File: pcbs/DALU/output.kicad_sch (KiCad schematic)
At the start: 5 parts, among them U601 74HCT541, U602 74HCT541, U603 74LS540, U604 74HCT541, U605 74HCT541

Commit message: Rethinking some design
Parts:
- removed U601, U602, U604, U605: 74HCT541, Package_DIP:DIP-20_W7.62mm_Socket, symbol 74xx:74HCT541
- removed U603: 74LS540, Package_DIP:DIP-20_W7.62mm_Socket, symbol 74xx:74LS540
- added R601: 10k, Resistor_THT:R_Axial_DIN0207_L6.3mm_D2.5mm_P7.62mm_Horizontal, symbol Device:R
- added RN601: R_Network08, Resistor_THT:R_Array_SIP9, symbol Device:R_Network08
- added U601: 74HC74, symbol 74xx:74HC74
- added U602: 74LS573, Package_DIP:DIP-20_W7.62mm_Socket, symbol 74xx:74LS573
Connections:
- net +5V: now also U601.1 (~{R}), U601.10 (~{S}), U601.13 (~{R}), U601.14 (VCC), U601.4 (~{S}), U602.20 (VCC)
- net GND: now also R601.2, RN601.1 (common), U601.11 (C), U601.12 (D), U601.7 (GND), U602.10 (GND)
- new net: U601.3 (C), U602.11 (Load)
- new net: RN601.9 (R8), U602.2 (D0)
- new net: RN601.8 (R7), U602.3 (D1)
- new net: RN601.7 (R6), U602.4 (D2)
- new net: RN601.6 (R5), U602.5 (D3)
- new net: RN601.5 (R4), U602.6 (D4)
- new net: RN601.4 (R3), U602.7 (D5)
- new net: RN601.3 (R2), U602.8 (D6)
- new net: RN601.2 (R1), U602.9 (D7)
- new net DALUFLAG: U601.5 (Q)
- new net FLAG: R601.1, U601.2 (D)
- no-connect marks 0 -> 3

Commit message: Thinking about some of the control logic
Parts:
- added D601, D602: 1N4148, Diode_THT:D_DO-35_SOD27_P7.62mm_Horizontal, symbol Diode:1N4148
- added R601, R603, R604: 100k, Resistor_THT:R_Axial_DIN0207_L6.3mm_D2.5mm_P7.62mm_Horizontal, symbol Device:R
- added R602: 10k, Resistor_THT:R_Axial_DIN0207_L6.3mm_D2.5mm_P7.62mm_Horizontal, symbol Device:R
- added U602: 74HC125, Package_DIP:DIP-14_W7.62mm_Socket, symbol 74xx:74LS125
- U601: footprint (none) -> Package_DIP:DIP-14_W7.62mm_Socket
- renumbered R601 to R605, U602 to U603
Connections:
- net +5V: now also R604.1, U602.14 (VCC), U602.5
- net GND: now also R601.2, R602.2, R603.1, U602.7 (GND)
- net CLK: now reaches U601.3 (C), U603.11 (Load)
- net CLK: now also R602.1, U602.3
- net at U603.1 (OE): now also R604.2, U602.8
- new net: D601.1 (K), D602.1 (K), R601.1, U602.4
- new net: R603.2, U602.10, U602.6
- new net Commit: D602.2 (A)
- new net Execute: D601.2 (A), U602.2
- new net ~{ACTIVE_{DALU}}: U602.1, U602.9
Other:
- note added: "Only one of Decode, Execute and Commit will be high at any given time"
- moved on the sheet: U601B

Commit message: Thinking about SMD assembly. Will be rethinking
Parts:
- removed U603: 74LS573, Package_DIP:DIP-20_W7.62mm_Socket, symbol 74xx:74LS573
- added U603: 74HCT574, Package_SO:SOIC-20W_7.5x12.8mm_P1.27mm, symbol 74xx:74HCT574
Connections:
- net +5V: now also U603.20 (VCC)
- net CLK: now also U603.11 (Cp)
- net GND: now also U603.10 (GND)
- net at R604.2, U602.8: now also U603.1 (OE)
- net at RN601.9 (R8): now also U603.2 (D0)
- net at RN601.8 (R7): now also U603.3 (D1)
- net at RN601.7 (R6): now also U603.4 (D2)
- net at RN601.6 (R5): now also U603.5 (D3)
- net at RN601.5 (R4): now also U603.6 (D4)
- net at RN601.4 (R3): now also U603.7 (D5)
- net at RN601.3 (R2): now also U603.8 (D6)
- net at RN601.2 (R1): now also U603.9 (D7)

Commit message: Doing some rethinking
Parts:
- U703: renamed from U603; footprint Package_SO:SOIC-20W_7.5x12.8mm_P1.27mm -> Package_DIP:DIP-20_W7.62mm_Socket; LCSC C435813 -> (none)
- renumbered D601 to D701, D602 to D702, R601 to R701, R602 to R702, R603 to R703, R604 to R704, R605 to R705, RN601 to RN701, U601 to U701, U602 to U702

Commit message: Starting to think about decoding etc.
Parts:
- removed D701, D702: 1N4148, Diode_THT:D_DO-35_SOD27_P7.62mm_Horizontal, symbol Diode:1N4148
- removed R701, R703, R704: 100k, Resistor_THT:R_Axial_DIN0207_L6.3mm_D2.5mm_P7.62mm_Horizontal, symbol Device:R
- removed R702: 10k, Resistor_THT:R_Axial_DIN0207_L6.3mm_D2.5mm_P7.62mm_Horizontal, symbol Device:R
- removed U702: 74HC125, Package_DIP:DIP-14_W7.62mm_Socket, symbol 74xx:74LS125
- renumbered R705 to R801, RN701 to RN801, U701 to U801, U703 to U802
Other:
- note removed: "Only one of Decode, Execute and Commit will be high at any given time"

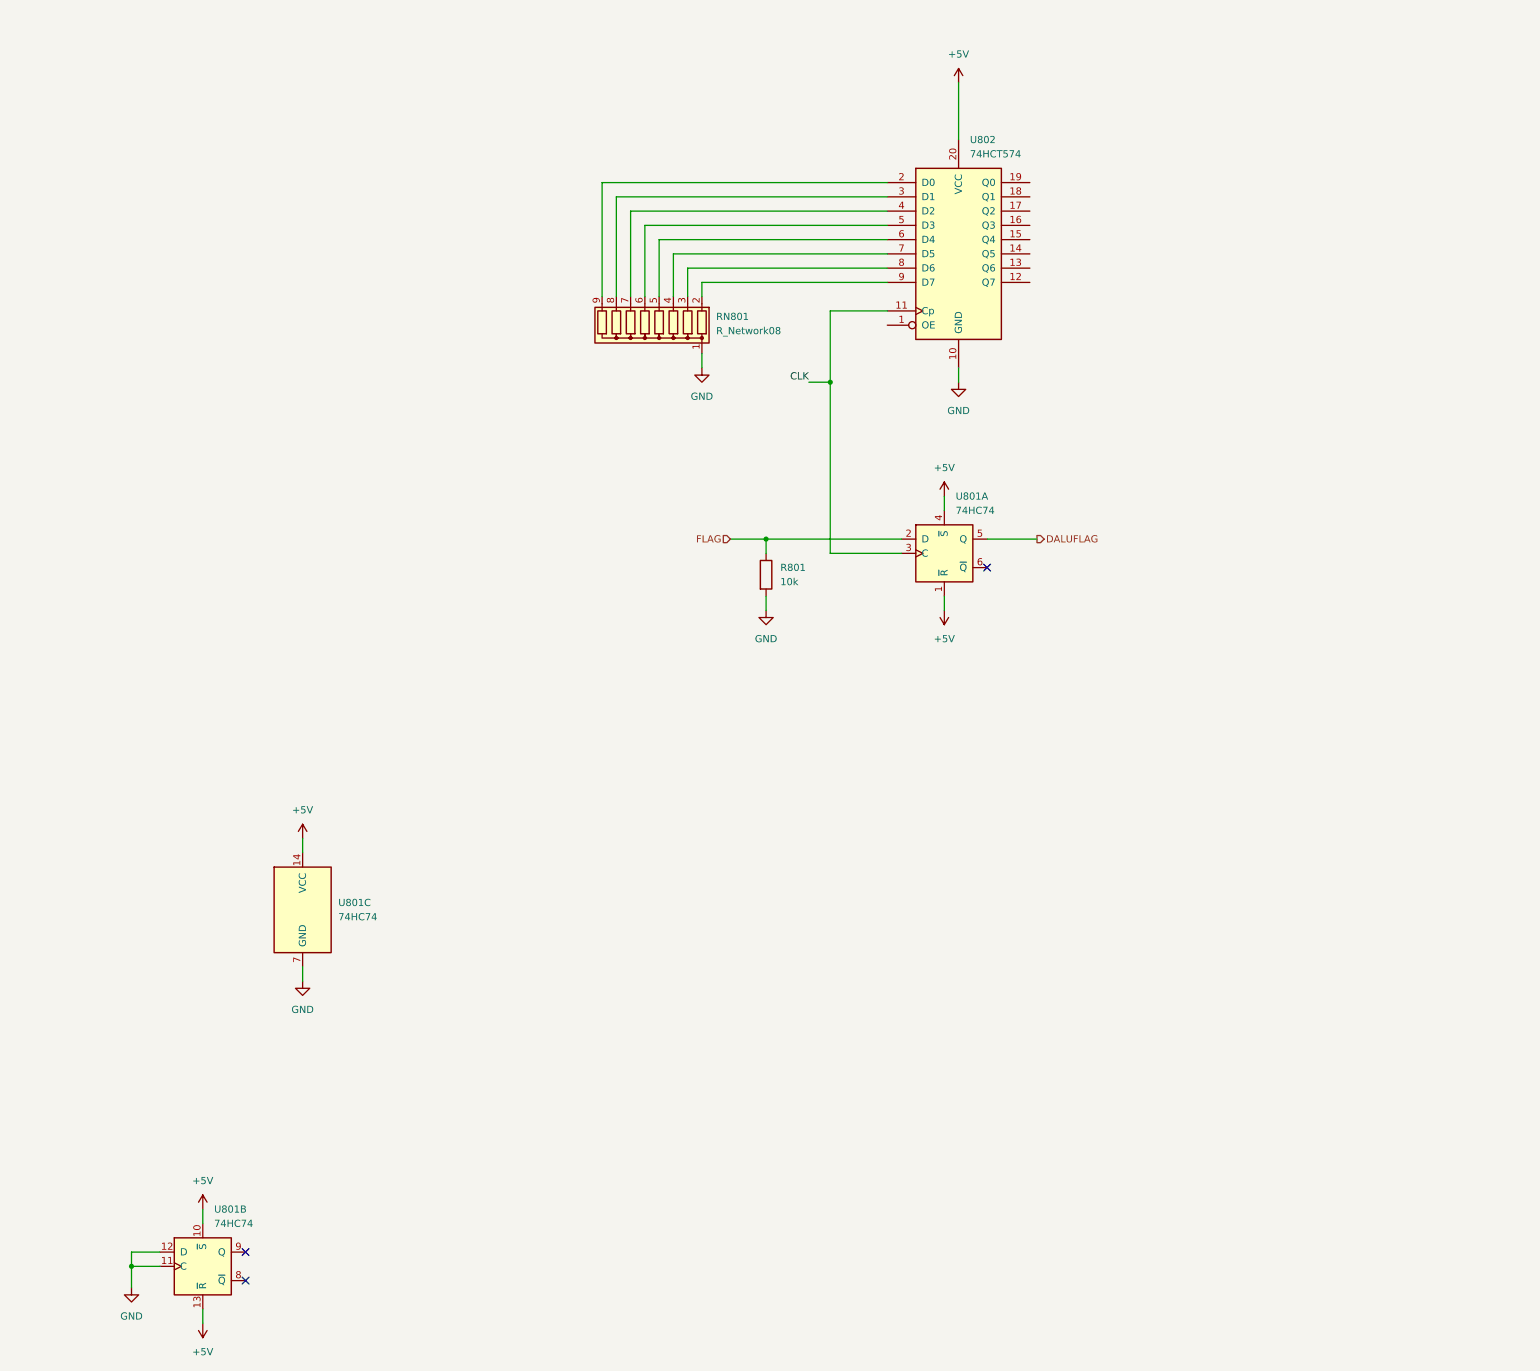
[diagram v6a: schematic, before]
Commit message: Starting to do the routing. Schematic not yet complete, though
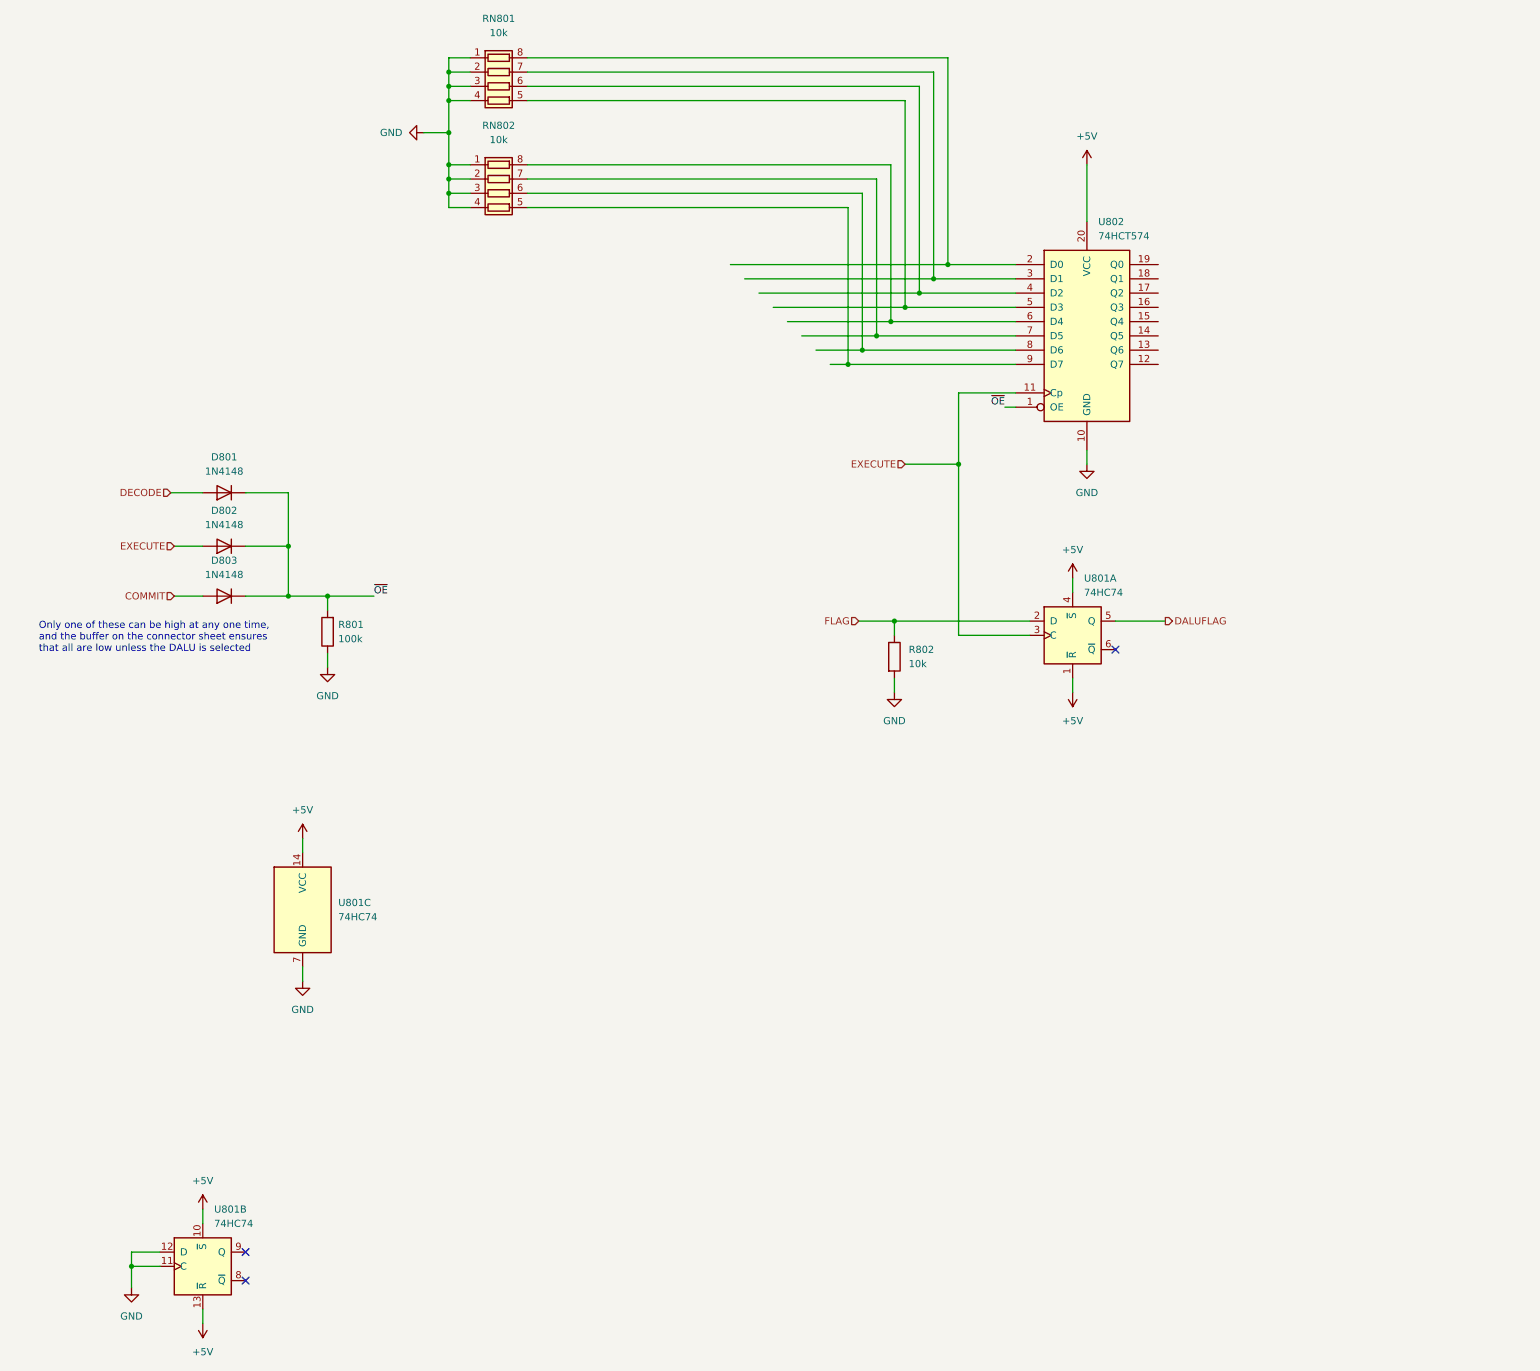
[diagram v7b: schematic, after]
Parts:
- removed RN801: R_Network08, Resistor_THT:R_Array_SIP9, symbol Device:R_Network08
- added D801, D802, D803: 1N4148, Diode_THT:D_DO-35_SOD27_P7.62mm_Horizontal, symbol Diode:1N4148
- added R801: 100k, Resistor_THT:R_Axial_DIN0207_L6.3mm_D2.5mm_P7.62mm_Horizontal, symbol Device:R
- added RN801, RN802: 10k, Resistor_SMD:R_Array_Convex_4x0402, symbol Device:R_Pack04
- renumbered R801 to R802
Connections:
- net GND: now also R801.1, RN801.1 (R1.1), RN801.2 (R2.1), RN801.3 (R3.1), RN801.4 (R4.1), RN802.1 (R1.1), RN802.2 (R2.1), RN802.3 (R3.1), RN802.4 (R4.1)
- net at U802.9 (D7): now also RN802.5 (R4.2)
- net at U802.8 (D6): now also RN802.6 (R3.2)
- net at U802.7 (D5): now also RN802.7 (R2.2)
- net at U802.6 (D4): now also RN802.8 (R1.2)
- net at U802.5 (D3): now also RN801.5 (R4.2)
- net at U802.4 (D2): now also RN801.6 (R3.2)
- net at U802.3 (D1): now also RN801.7 (R2.2)
- net at U802.2 (D0): now also RN801.8 (R1.2)
- net ~{OE}: now reaches U802.1 (OE)
- net ~{OE}: now also D801.1 (K), D802.1 (K), D803.1 (K), R801.2
- net CLK renamed EXECUTE
- net EXECUTE: now also D802.2 (A)
- new net COMMIT: D803.2 (A)
- new net DECODE: D801.2 (A)
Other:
- note added: "Only one of these can be high at any one time, and the buffer on the connector sheet ensures that all are low unless the DALU is selected"
- moved on the sheet: R802, U801A, U802

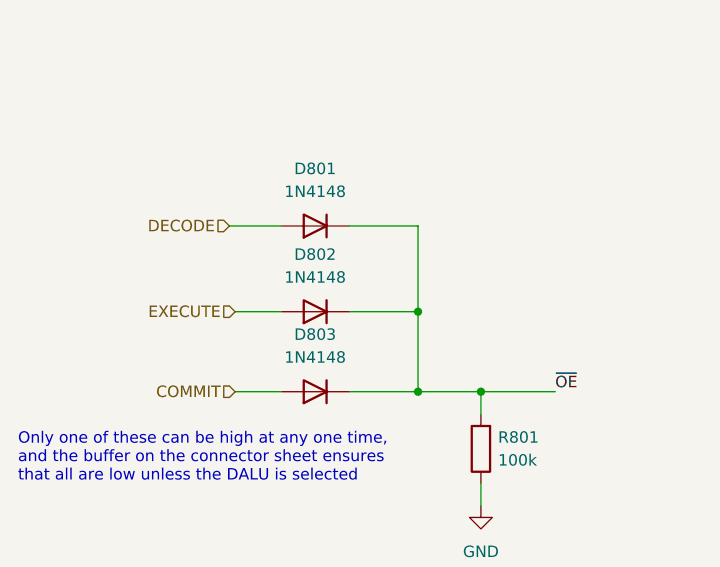
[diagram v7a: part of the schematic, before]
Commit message: Removing diode ORs (mainly). Preparing for a small rethink
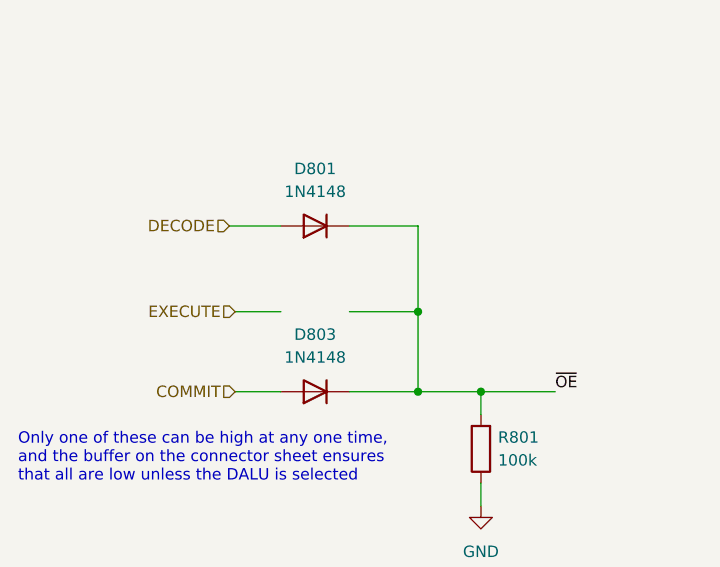
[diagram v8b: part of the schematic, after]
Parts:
- removed D802: 1N4148, Diode_THT:D_DO-35_SOD27_P7.62mm_Horizontal, symbol Diode:1N4148
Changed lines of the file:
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@@
-    (pin "2")
-  )
-  (symbol (lib_id "Diode:1N4148") (at 49.53 107.95 180) (unit 1)
-    (in_bom yes) (on_board yes) (fields_autoplaced)
-    (property "Reference" "D802" (id 0) (at 49.53 101.6 0))
-    (property "Value" "1N4148" (id 1) (at 49.53 104.14 0))
-    (property "Footprint" "Diode_THT:D_DO-35_SOD27_P7.62mm_Horizontal" (id 2) (at 49.53 107.95 0)
-      (effects (font (size 1.27 1.27)) hide)
-    )
-    (property "Datasheet" "https://assets.nexperia.com/documents/data-sheet/1N4148_1N4448.pdf" (id 3) (at 49.53 107.95 0)
-      (effects (font (size 1.27 1.27)) hide)
-    )
-    (pin "1")
     (pin "2")
   )
